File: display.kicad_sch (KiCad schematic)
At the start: 53 parts, among them Q23 BSS83P, Q24 BSS83P, Q25 BSS83P, Q26 BSS83P, Q27 BSS83P, Q28 BSS83P, Q29 BSS83P, Q30 BSS83P, Q31 2N7002K, Q32 2N7002K, Q33 2N7002K, Q34 2N7002K, Q35 2N7002K, Q36 2N7002K, Q37 2N7002K, Q38 2N7002K, U7 74HC595, U8 74HC595, U9 CC56-12GWA

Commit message: Page reordering
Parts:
- renumbered C210 to C207, C211 to C208, D5 to D1, D6 to D2, D7 to D3, D8 to D4, Q26 to Q10, Q27 to Q11, Q28 to Q12, Q29 to Q13, Q30 to Q14, Q33 to Q15, Q31 to Q16, Q32 to Q17, Q34 to Q18, Q35 to Q19, Q36 to Q20, Q37 to Q21, Q38 to Q22, Q23 to Q7, Q24 to Q8, Q25 to Q9, R207 to R206, R237 to R209, R250 to R210, R251 to R213, R252 to R214, R253 to R215, R254 to R227, R255 to R228, R266 to R229, R264 to R230, R265 to R231, R267 to R232, R268 to R233, R270 to R234, R272 to R235, R274 to R236, R256 to R238, R257 to R239, R258 to R240, R259 to R241, R260 to R242, R261 to R243, R262 to R244, R263 to R245, R269 to R246, R271 to R247, R273 to R248, R275 to R249, U8 to U4

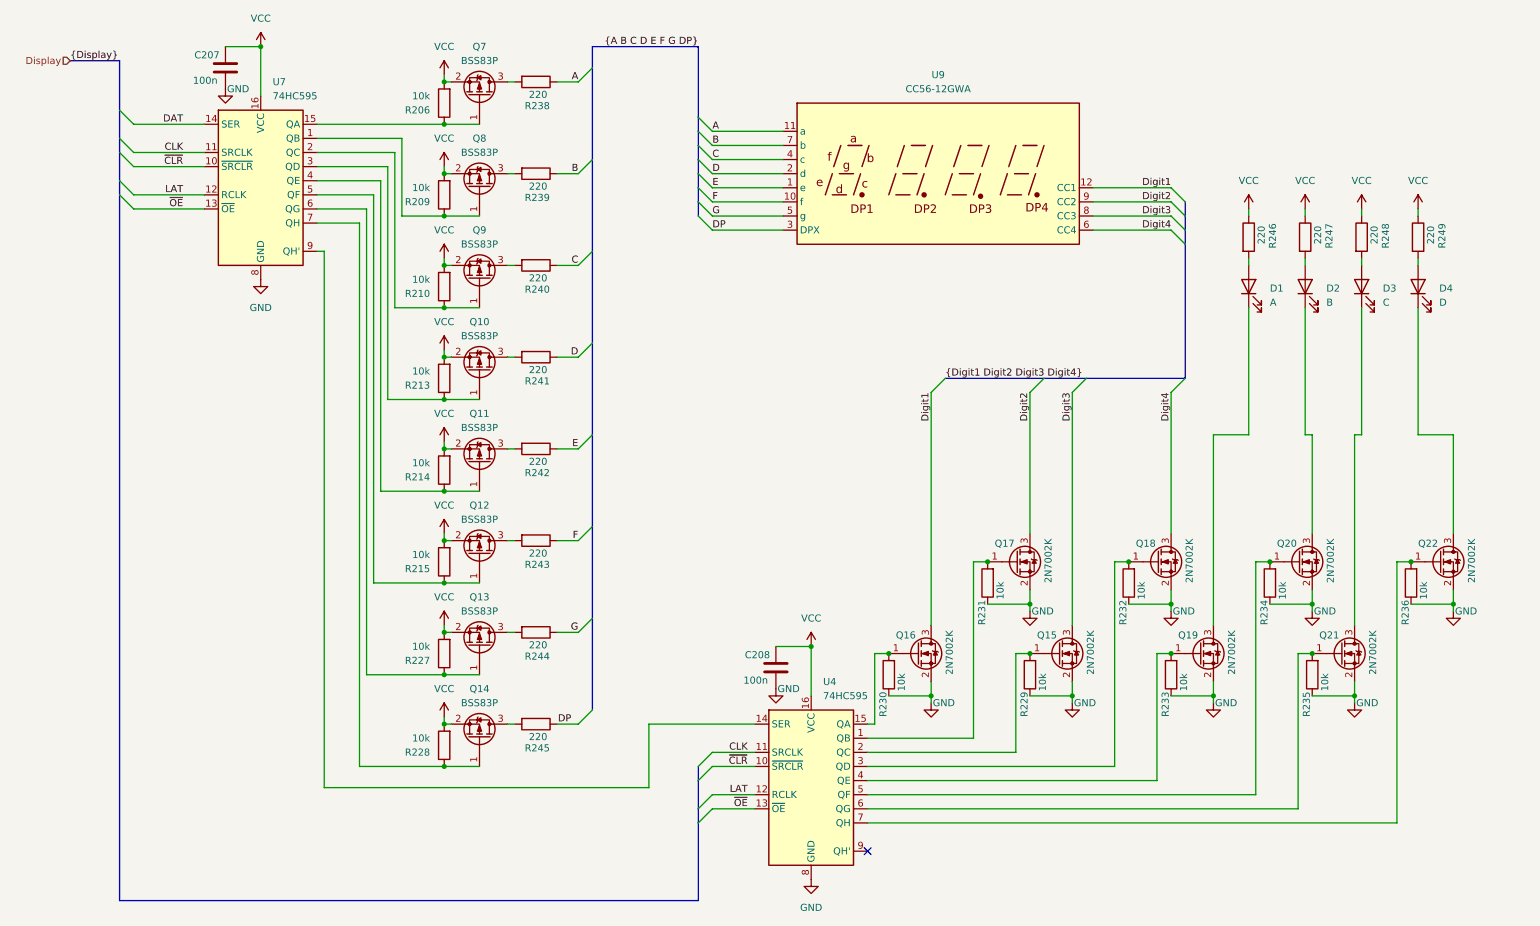
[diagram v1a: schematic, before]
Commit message: Assign component LCSC part numbers
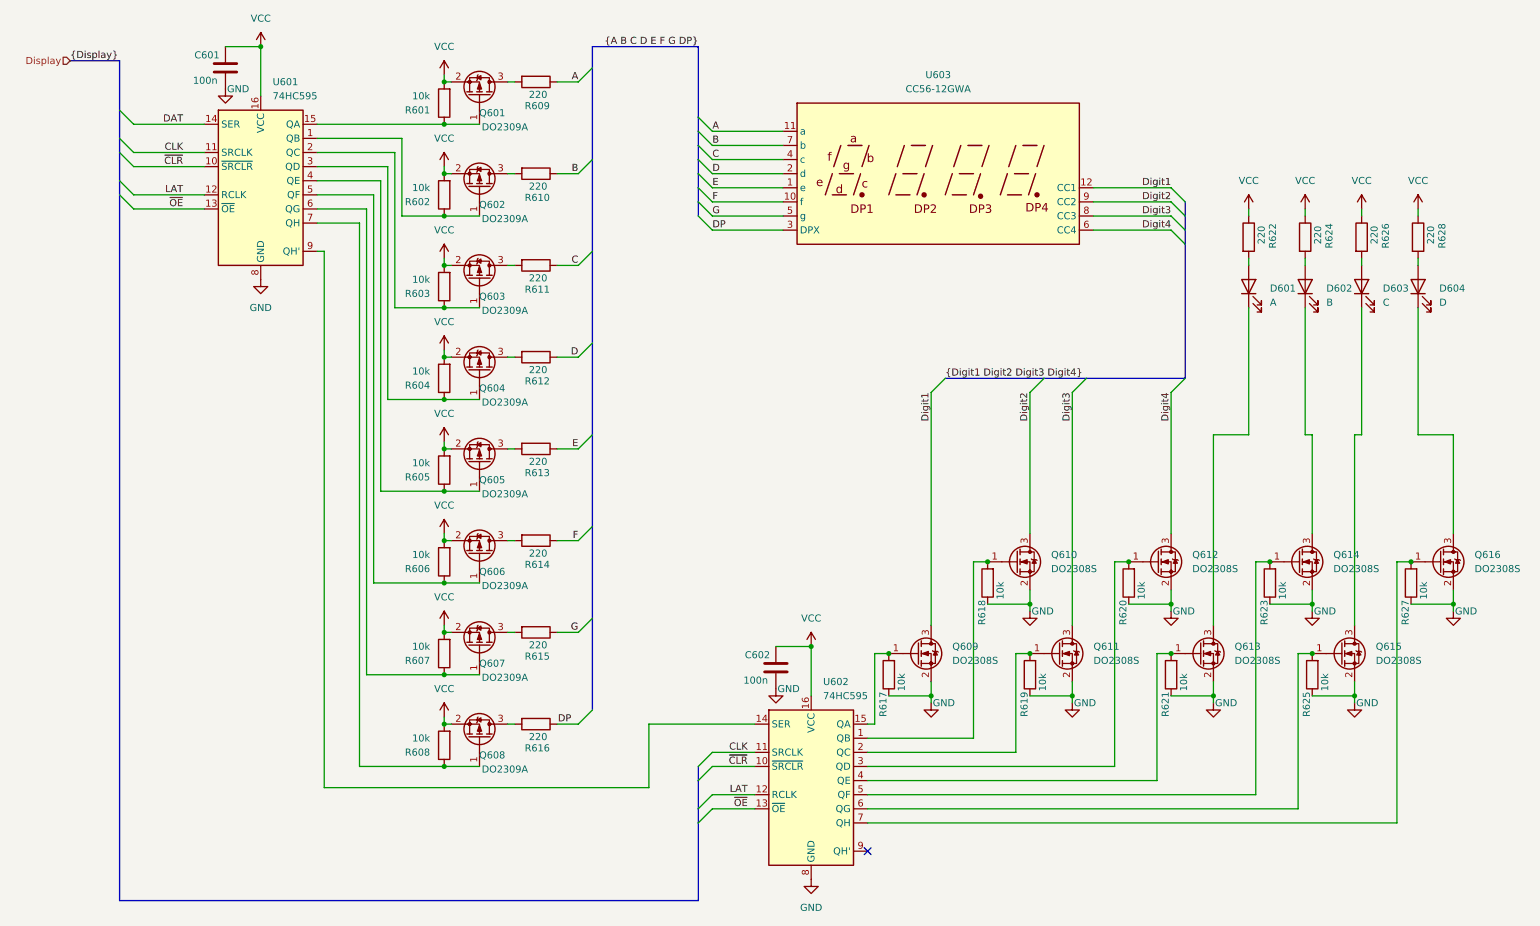
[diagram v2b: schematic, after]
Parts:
- removed Q10, Q11, Q12, Q13, Q14, Q7, Q8, Q9: BSS83P, Package_TO_SOT_SMD:SOT-23, symbol Transistor_FET:BSS83P
- removed Q15, Q16, Q17, Q18, Q19, Q20, Q21, Q22: 2N7002K, Package_TO_SOT_SMD:SOT-23, symbol Transistor_FET:2N7002K
- added Q601, Q602, Q603, Q604, Q605, Q606, Q607, Q608: DO2309A, Package_TO_SOT_SMD:SOT-23_Handsoldering, symbol Transistor_FET:BSS83P
- added Q609, Q610, Q611, Q612, Q613, Q614, Q615, Q616: DO2308S, Package_TO_SOT_SMD:SOT-23_Handsoldering, symbol Transistor_FET:2N7002K
- D601: renamed from D1; footprint (none) -> LED_SMD:LED_1206_3216Metric_Pad1.42x1.75mm_HandSolder
- D602: renamed from D2; footprint (none) -> LED_SMD:LED_1206_3216Metric_Pad1.42x1.75mm_HandSolder
- D603: renamed from D3; footprint (none) -> LED_SMD:LED_1206_3216Metric_Pad1.42x1.75mm_HandSolder
- D604: renamed from D4; footprint (none) -> LED_SMD:LED_1206_3216Metric_Pad1.42x1.75mm_HandSolder
- U601: renamed from U7; footprint (none) -> Package_SO:SOIC-16_3.9x9.9mm_P1.27mm; LCSC (none) -> C110383
- U602: renamed from U4; footprint (none) -> Package_SO:SOIC-16_3.9x9.9mm_P1.27mm; LCSC (none) -> C110383
- U603: renamed from U9; LCSC (none) -> C109200
- renumbered C207 to C601, C208 to C602, R206 to R601, R209 to R602, R210 to R603, R213 to R604, R214 to R605, R215 to R606, R227 to R607, R228 to R608, R238 to R609, R239 to R610, R240 to R611, R241 to R612, R242 to R613, R243 to R614, R244 to R615, R245 to R616, R230 to R617, R231 to R618, R229 to R619, R232 to R620, R233 to R621, R246 to R622, R234 to R623, R247 to R624, R235 to R625, R248 to R626, R236 to R627, R249 to R628
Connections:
- net Digit1: now also Q609.3 (D)
- net Digit2: now also Q610.3 (D)
- net Digit3: now also Q611.3 (D)
- net Digit4: now also Q612.3 (D)
- net GND: now also Q609.2 (S), Q610.2 (S), Q611.2 (S), Q612.2 (S), Q613.2 (S), Q614.2 (S), Q615.2 (S), Q616.2 (S)
- net VCC: now also Q601.2 (S), Q602.2 (S), Q603.2 (S), Q604.2 (S), Q605.2 (S), Q606.2 (S), Q607.2 (S), Q608.2 (S)
- net at R601.1, U601.15 (QA): now also Q601.1 (G)
- net at R609.2: now also Q601.3 (D)
- net at R620.2, U602.3 (QD): now also Q612.1 (G)
- net at R611.2: now also Q603.3 (D)
- net at R602.1, U601.1 (QB): now also Q602.1 (G)
- net at R610.2: now also Q602.3 (D)
- net at R625.2, U602.6 (QG): now also Q615.1 (G)
- net at R615.2: now also Q607.3 (D)
- net at R617.2, U602.15 (QA): now also Q609.1 (G)
- net at R605.1, U601.4 (QE): now also Q605.1 (G)
- net at R603.1, U601.2 (QC): now also Q603.1 (G)
- net at R604.1, U601.3 (QD): now also Q604.1 (G)
- net at R606.1, U601.5 (QF): now also Q606.1 (G)
- net at R607.1, U601.6 (QG): now also Q607.1 (G)
- net at R608.1, U601.7 (QH): now also Q608.1 (G)
- net at R612.2: now also Q604.3 (D)
- net at R627.2, U602.7 (QH): now also Q616.1 (G)
- net at R619.2, U602.2 (QC): now also Q611.1 (G)
- net at R616.2: now also Q608.3 (D)
- net at R618.2, U602.1 (QB): now also Q610.1 (G)
- net at R621.2, U602.4 (QE): now also Q613.1 (G)
- net at D601.1 (K): now also Q613.3 (D)
- net at D604.1 (K): now also Q616.3 (D)
- net at D602.1 (K): now also Q614.3 (D)
- net at R623.2, U602.5 (QF): now also Q614.1 (G)
- net at R613.2: now also Q605.3 (D)
- net at D603.1 (K): now also Q615.3 (D)
- net at R614.2: now also Q606.3 (D)

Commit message: Simplify some schematics to reduce BOM
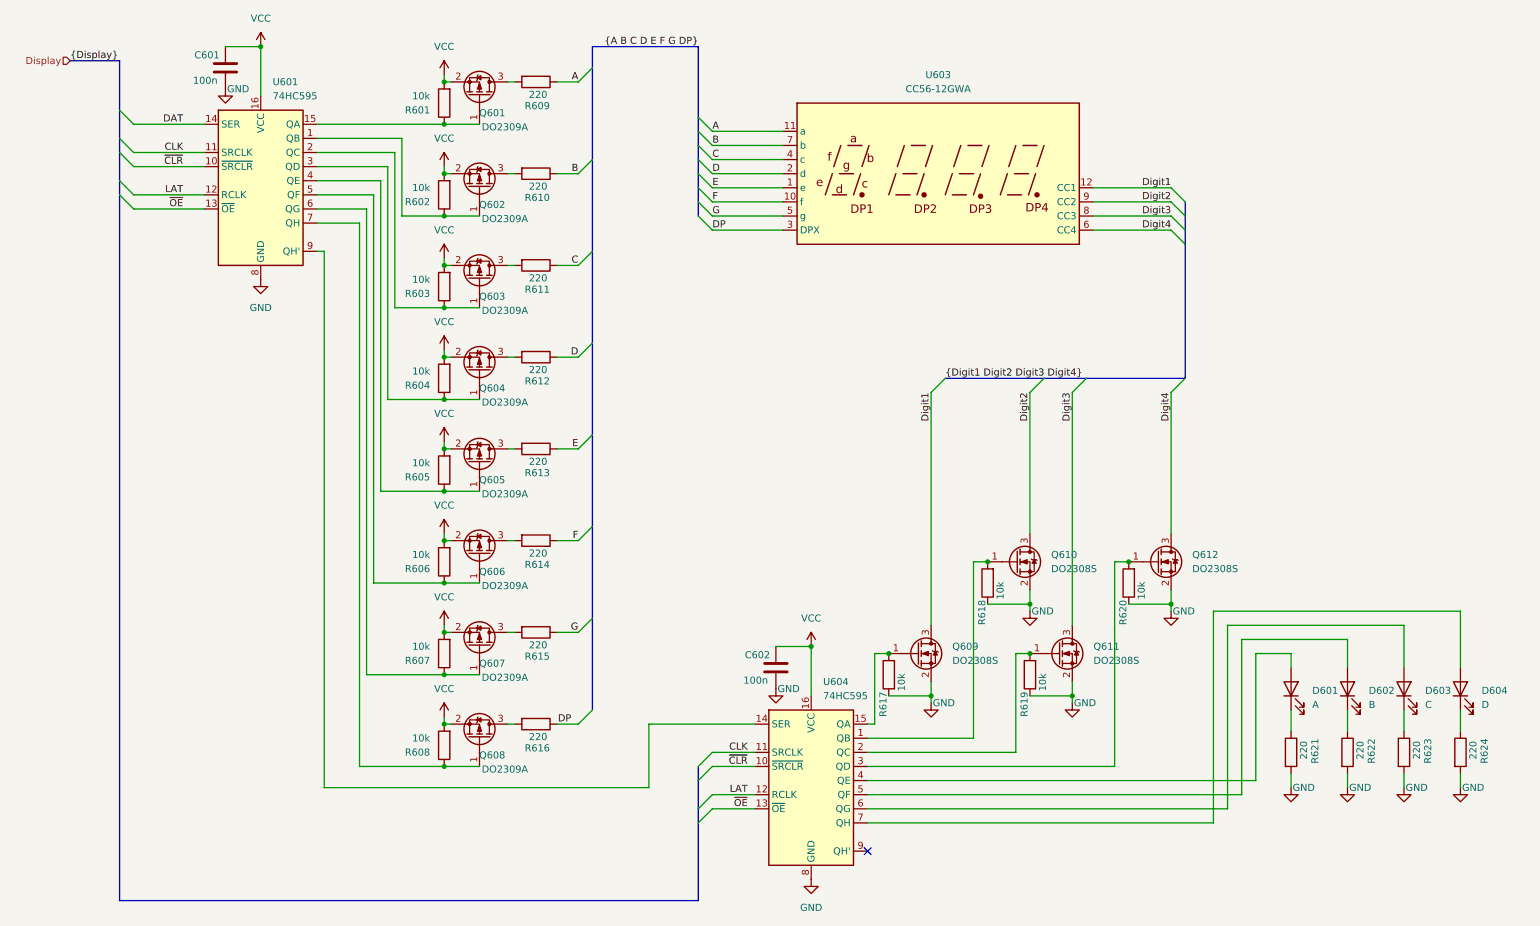
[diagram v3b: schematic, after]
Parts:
- removed Q613, Q614, Q615, Q616: DO2308S, Package_TO_SOT_SMD:SOT-23_Handsoldering, symbol Transistor_FET:2N7002K
- removed R621, R623, R625, R627: 10k, Resistor_SMD:R_1206_3216Metric_Pad1.30x1.75mm_HandSolder, symbol Device:R
- removed U602: 74HC595, Package_SO:SOIC-16_3.9x9.9mm_P1.27mm, symbol 74xx:74HC595
- added U604: 74HC595, Package_SO:SOIC-16_3.9x9.9mm_P1.27mm, symbol 74xx:74HC595
- U601: LCSC C110383 -> C10092
- renumbered R622 to R621, R624 to R622, R626 to R623, R628 to R624
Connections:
- net CLK: now also U604.11 (SRCLK)
- net GND: now also R621.2, R622.2, R623.2, R624.2, U604.8 (GND)
- net LAT: now also U604.12 (RCLK)
- net VCC: now also U604.16 (VCC); no longer R621.1, R622.1, R623.1, R624.1
- net ~{CLR}: now also U604.10 (~{SRCLR})
- net ~{OE}: now also U604.13 (~{OE})
- net at D602.2 (A): now also U604.5 (QF); no longer R622.2
- net at Q609.1 (G), R617.2: now also U604.15 (QA)
- net at Q612.1 (G), R620.2: now also U604.3 (QD)
- net at U601.9 (QH'): now also U604.14 (SER)
- net at D602.1 (K): now also R622.1
- net at Q611.1 (G), R619.2: now also U604.2 (QC)
- net at Q610.1 (G), R618.2: now also U604.1 (QB)
- net at D601.1 (K): now also R621.1
- net at D601.2 (A): now also U604.4 (QE); no longer R621.2
- net at D604.1 (K): now also R624.1
- net at D604.2 (A): now also U604.7 (QH); no longer R624.2
- net at D603.2 (A): now also U604.6 (QG); no longer R623.2
- net at D603.1 (K): now also R623.1
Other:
- moved on the sheet: D601, D602, D603, D604, R621, R622, R623, R624

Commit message: Subcircuits routed
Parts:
- added TP601: DAT, TestPoint:TestPoint_Pad_D1.0mm, symbol Connector:TestPoint
- added TP602: CLK, TestPoint:TestPoint_Pad_D1.0mm, symbol Connector:TestPoint
- added TP603: ~CLR, TestPoint:TestPoint_Pad_D1.0mm, symbol Connector:TestPoint
- added TP604: LAT, TestPoint:TestPoint_Pad_D1.0mm, symbol Connector:TestPoint
- added TP605: ~OE, TestPoint:TestPoint_Pad_D1.0mm, symbol Connector:TestPoint
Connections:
- net CLK: now also TP602.1
- net DAT: now also TP601.1
- net LAT: now also TP604.1
- net ~{CLR}: now also TP603.1
- net ~{OE}: now also TP605.1
